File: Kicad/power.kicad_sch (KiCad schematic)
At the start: 34 parts, among them J7 22112042

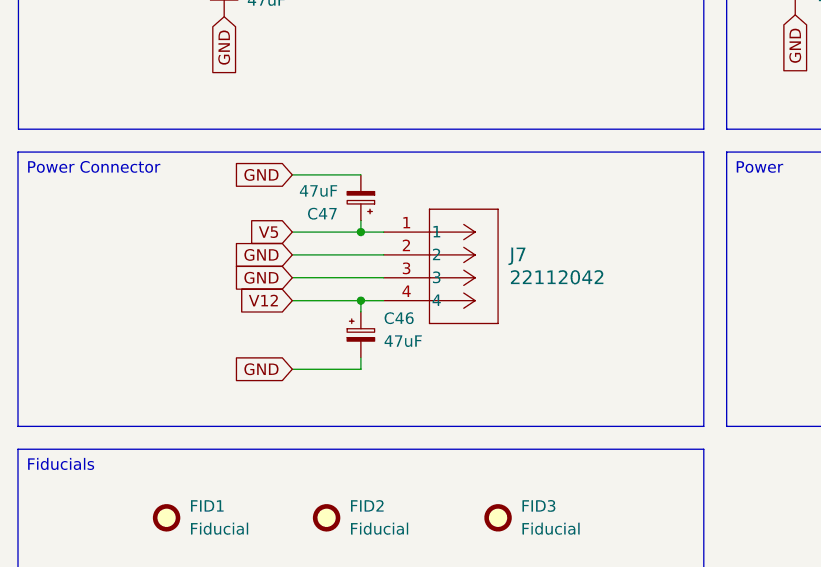
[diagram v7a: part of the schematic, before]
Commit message: Add bypass cap for Berg connector
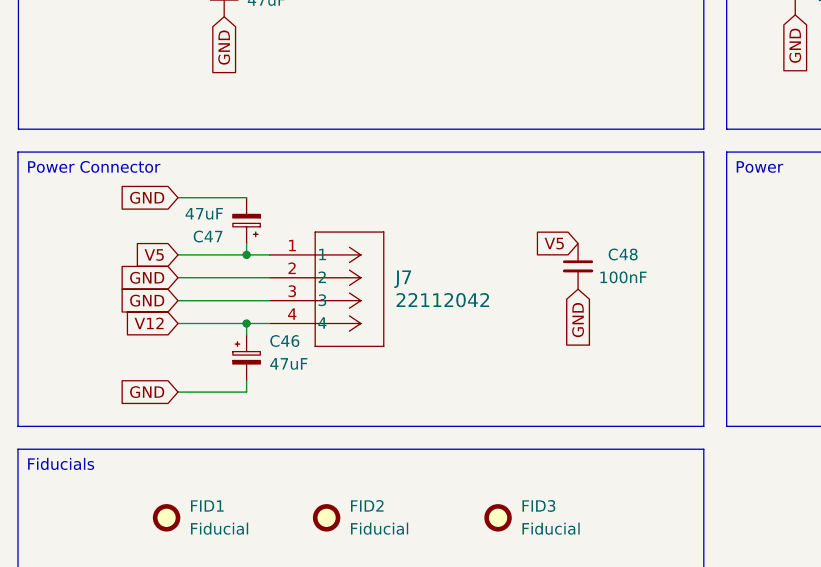
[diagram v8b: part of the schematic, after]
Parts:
- added C48: 100nF, Capacitor_SMD:C_0603_1608Metric_Pad1.08x0.95mm_HandSolder, symbol Device:C_Small
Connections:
- net +5V: now also C48.1
- net GND: now also C48.2
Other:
- moved on the sheet: C46, C47, J7
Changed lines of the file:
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@@
 	)
 	(junction
-		(at 58.42 118.11)
+		(at 45.72 120.65)
 		(diameter 0)
 		(color 0 0 0 0)
@@
 	)
 	(junction
-		(at 58.42 125.73)
+		(at 45.72 128.27)
 		(diameter 0)
 		(color 0 0 0 0)
@@
 	(wire
 		(pts
-			(xy 50.8 133.35) (xy 58.42 133.35)
+			(xy 38.1 135.89) (xy 45.72 135.89)
 		)
 		(stroke
@@
 	(wire
 		(pts
-			(xy 50.8 125.73) (xy 58.42 125.73)
+			(xy 38.1 128.27) (xy 45.72 128.27)
 		)
 		(stroke
@@
 	(wire
 		(pts
-			(xy 58.42 116.84) (xy 58.42 118.11)
+			(xy 45.72 119.38) (xy 45.72 120.65)
 		)
 		(stroke
@@
 	(wire
 		(pts
-			(xy 58.42 125.73) (xy 60.96 125.73)
+			(xy 45.72 128.27) (xy 48.26 128.27)
 		)
 		(stroke
@@
 	(wire
 		(pts
-			(xy 58.42 118.11) (xy 60.96 118.11)
+			(xy 45.72 120.65) (xy 48.26 120.65)
 		)
 		(stroke
@@
 	(wire
 		(pts
-			(xy 50.8 120.65) (xy 60.96 120.65)
+			(xy 38.1 123.19) (xy 48.26 123.19)
 		)
 		(stroke
@@
 	(wire
 		(pts
-			(xy 58.42 133.35) (xy 58.42 132.08)
+			(xy 45.72 135.89) (xy 45.72 134.62)
 		)
 		(stroke
@@
 	(wire
 		(pts
-			(xy 50.8 123.19) (xy 60.96 123.19)
+			(xy 38.1 125.73) (xy 48.26 125.73)
 		)
 		(stroke
@@
 	(wire
 		(pts
-			(xy 50.8 118.11) (xy 58.42 118.11)
+			(xy 38.1 120.65) (xy 45.72 120.65)
 		)
 		(stroke
@@
 	(wire
 		(pts
-			(xy 58.42 127) (xy 58.42 125.73)
+			(xy 45.72 129.54) (xy 45.72 128.27)
 		)
 		(stroke
@@
 	(wire
 		(pts
-			(xy 50.8 111.76) (xy 58.42 111.76)
+			(xy 38.1 114.3) (xy 45.72 114.3)
 		)
 		(stroke
@@
 	(global_label "V5"
 		(shape input)
-		(at 50.8 118.11 180)
+		(at 38.1 120.65 180)
 		(fields_autoplaced yes)
 		(effects
@@
 		)
 		(property "Intersheetrefs" "${INTERSHEET_REFS}"
-			(at 45.5167 118.11 0)
+			(at 32.8167 120.65 0)
 			(effects
 				(font
@@
 	(global_label "GND"
 		(shape input)
-		(at 50.8 133.35 180)
+		(at 38.1 135.89 180)
 		(fields_autoplaced yes)
 		(effects
@@
 		)
 		(property "Intersheetrefs" "${INTERSHEET_REFS}"
-			(at 43.9443 133.35 0)
+			(at 31.2443 135.89 0)
 			(effects
 				(font
@@
 	(global_label "GND"
 		(shape input)
-		(at 50.8 120.65 180)
+		(at 38.1 123.19 180)
 		(fields_autoplaced yes)
 		(effects
@@
 		)
 		(property "Intersheetrefs" "${INTERSHEET_REFS}"
-			(at 43.9443 120.65 0)
+			(at 31.2443 123.19 0)
+			(effects
+				(font
+					(size 1.27 1.27)
+				)
+				(justify right)
+				(hide yes)
+			)
+		)
+	)
+	(global_label "GND"
+		(shape input)
+		(at 82.55 124.46 270)
+		(fields_autoplaced yes)
+		(effects
+			(font
+				(size 1.27 1.27)
+			)
+			(justify right)
+		)
+		(property "Intersheetrefs" "${INTERSHEET_REFS}"
+			(at 82.55 131.3157 90)
 			(effects
 				(font
@@
 	(global_label "GND"
 		(shape input)
-		(at 50.8 111.76 180)
+		(at 38.1 114.3 180)
 		(fields_autoplaced yes)
 		(effects
@@
 		)
 		(property "Intersheetrefs" "${INTERSHEET_REFS}"
-			(at 43.9443 111.76 0)
+			(at 31.2443 114.3 0)
 			(effects
 				(font
@@
 	(global_label "V5"
 		(shape input)
+		(at 82.55 119.38 180)
+		(fields_autoplaced yes)
+		(effects
+			(font
+				(size 1.27 1.27)
+			)
+			(justify right)
+		)
+		(property "Intersheetrefs" "${INTERSHEET_REFS}"
+			(at 77.2667 119.38 0)
+			(effects
+				(font
+					(size 1.27 1.27)
+				)
+				(justify right)
+				(hide yes)
+			)
+		)
+	)
+	(global_label "V5"
+		(shape input)
 		(at 39.37 27.94 180)
 		(fields_autoplaced yes)
@@
 	(global_label "GND"
 		(shape input)
-		(at 50.8 123.19 180)
+		(at 38.1 125.73 180)
 		(fields_autoplaced yes)
 		(effects
@@
 		)
 		(property "Intersheetrefs" "${INTERSHEET_REFS}"
-			(at 43.9443 123.19 0)
+			(at 31.2443 125.73 0)
 			(effects
 				(font
@@
 	(global_label "V12"
 		(shape input)
-		(at 50.8 125.73 180)
+		(at 38.1 128.27 180)
 		(fields_autoplaced yes)
 		(effects
@@
 		)
 		(property "Intersheetrefs" "${INTERSHEET_REFS}"
-			(at 44.3072 125.73 0)
+			(at 31.6072 128.27 0)
 			(effects
 				(font
@@
 	(symbol
 		(lib_id "Device:C_Small")
+		(at 82.55 121.92 0)
+		(unit 1)
+		(exclude_from_sim no)
+		(in_bom yes)
+		(on_board yes)
+		(dnp no)
+		(property "Reference" "C48"
+			(at 85.852 120.65 0)
+			(effects
+				(font
+					(size 1.27 1.27)
+				)
+				(justify left)
+			)
+		)
+		(property "Value" "100nF"
+			(at 84.836 123.19 0)
+			(effects
+				(font
+					(size 1.27 1.27)
+				)
+				(justify left)
+			)
+		)
+		(property "Footprint" "Capacitor_SMD:C_0603_1608Metric_Pad1.08x0.95mm_HandSolder"
+			(at 82.55 121.92 0)
+			(effects
+				(font
+					(size 1.27 1.27)
+				)
+				(hide yes)
+			)
+		)
+		(property "Datasheet" "~"
+			(at 82.55 121.92 0)
+			(effects
+				(font
+					(size 1.27 1.27)
+				)
+				(hide yes)
+			)
+		)
+		(property "Description" "Unpolarized capacitor, small symbol"
+			(at 82.55 121.92 0)
+			(effects
+				(font
+					(size 1.27 1.27)
+				)
+				(hide yes)
+			)
+		)
+		(property "LCSC Part #" "C14663"
+			(at 82.55 121.92 0)
+			(effects
+				(font
+					(size 1.27 1.27)
+				)
+				(hide yes)
+			)
+		)
+		(pin "2"
+		)
+		(pin "1"
+		)
+		(instances
+			(project "A4092"
+				(path "/8f9f4021-47aa-41d9-bea7-f6ccf72098bb/166c366c-e5f9-4398-87d9-75fc4b57be99"
+					(reference "C48")
+					(unit 1)
+				)
+			)
+		)
+	)
+	(symbol
+		(lib_id "Device:C_Small")
 		(at 86.36 30.48 0)
 		(unit 1)
@@
 	(symbol
 		(lib_id "Device:C_Polarized_Small")
-		(at 58.42 129.54 0)
+		(at 45.72 132.08 0)
 		(unit 1)
 		(exclude_from_sim no)
@@
 		(fields_autoplaced yes)
 		(property "Reference" "C46"
-			(at 60.96 127.7238 0)
+			(at 48.26 130.2638 0)
 			(effects
 				(font
@@
 		)
 		(property "Value" "47uF"
-			(at 60.96 130.2638 0)
+			(at 48.26 132.8038 0)
 			(effects
 				(font
@@
 		)
 		(property "Footprint" "Capacitor_SMD:CP_Elec_6.3x7.7"
-			(at 58.42 129.54 0)
+			(at 45.72 132.08 0)
 			(effects
 				(font
@@
 		)
 		(property "Datasheet" "~"
-			(at 58.42 129.54 0)
+			(at 45.72 132.08 0)
 			(effects
 				(font
@@
 		)
 		(property "Description" "Polarized capacitor, small symbol"
-			(at 58.42 129.54 0)
+			(at 45.72 132.08 0)
 			(effects
 				(font
@@
 		)
 		(property "MPN" "KEMET/A765EB476M1ELAE040"
-			(at 58.42 129.54 0)
+			(at 45.72 132.08 0)
 			(effects
 				(font
@@
 		)
 		(property "LCSC Part #" "C369909"
-			(at 58.42 129.54 0)
+			(at 45.72 132.08 0)
 			(effects
 				(font
@@
 	(symbol
 		(lib_id "Device:C_Polarized_Small")
-		(at 58.42 114.3 180)
+		(at 45.72 116.84 180)
 		(unit 1)
 		(exclude_from_sim no)
@@
 		(fields_autoplaced yes)
 		(property "Reference" "C47"
-			(at 55.88 116.1162 0)
+			(at 43.18 118.6562 0)
 			(effects
 				(font
@@
 		)
 		(property "Value" "47uF"
-			(at 55.88 113.5762 0)
+			(at 43.18 116.1162 0)
 			(effects
 				(font
@@
 		)
 		(property "Footprint" "Capacitor_SMD:CP_Elec_6.3x7.7"
-			(at 58.42 114.3 0)
+			(at 45.72 116.84 0)
 			(effects
 				(font
@@
 		)
 		(property "Datasheet" "~"
-			(at 58.42 114.3 0)
+			(at 45.72 116.84 0)
 			(effects
 				(font
@@
 		)
 		(property "Description" "Polarized capacitor, small symbol"
-			(at 58.42 114.3 0)
+			(at 45.72 116.84 0)
 			(effects
 				(font
@@
 		)
 		(property "MPN" "KEMET/A765EB476M1ELAE040"
-			(at 58.42 114.3 0)
+			(at 45.72 116.84 0)
 			(effects
 				(font
@@
 		)
 		(property "LCSC Part #" "C369909"
-			(at 58.42 114.3 0)
+			(at 45.72 116.84 0)
 			(effects
 				(font
@@
 	(symbol
 		(lib_id "22112042:22112042")
-		(at 60.96 118.11 0)
+		(at 48.26 120.65 0)
 		(unit 1)
 		(exclude_from_sim no)
@@
 		(fields_autoplaced yes)
 		(property "Reference" "J7"
-			(at 74.93 120.6499 0)
+			(at 62.23 123.1899 0)
 			(effects
 				(font
@@
 		)
 		(property "Value" "22112042"
-			(at 74.93 123.1899 0)
+			(at 62.23 125.7299 0)
 			(effects
 				(font
@@
 		)
 		(property "Footprint" "22112042:CONN_A-6373-04A_MOL"
-			(at 60.96 118.11 0)
+			(at 48.26 120.65 0)
 			(effects
 				(font
@@
 		)
 		(property "Datasheet" "22112042"
-			(at 60.96 118.11 0)
+			(at 48.26 120.65 0)
 			(effects
 				(font
@@
 		)
 		(property "Description" ""
-			(at 60.96 118.11 0)
+			(at 48.26 120.65 0)
 			(effects
 				(font
@@
 		)
 		(property "LCSC Part #" "C114123"
-			(at 60.96 118.11 0)
+			(at 48.26 120.65 0)
 			(effects
 				(font
